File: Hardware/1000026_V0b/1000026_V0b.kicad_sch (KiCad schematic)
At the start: 29 parts, among them J1 533750410, J2 4390, J3 532580229, J5 532580229, J9 0525591853, SW1 TL3305CF260QG, U1 BD450M5FP-CE2, U2 MAX7480ESA+

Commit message: Updating lp filter test project
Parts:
- D1, D2: footprint RobotFtpLib:1N4007G-T -> DO-41_DIO
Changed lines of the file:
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@@
 			)
 		)
-		(property "Footprint" "RobotFtpLib:1N4007G-T"
+		(property "Footprint" "DO-41_DIO"
 			(at 95.504 127.381 0)
 			(effects
@@
 	)
 	(symbol
-		(lib_name "1N4007G-T_1")
 		(lib_id "RobotSymLib:1N4007G-T")
 		(at 93.7859 110.2875 0)
@@
 			)
 		)
-		(property "Footprint" "RobotFtpLib:1N4007G-T"
+		(property "Footprint" "DO-41_DIO"
 			(at 99.1199 103.6835 0)
 			(effects
@@
 			)
 		)
-		(property "Description" ""
+		(property "Description" "Power symbol creates a global label with name \"+7.4V\""
 			(at 23.8954 151.3699 0)
 			(effects

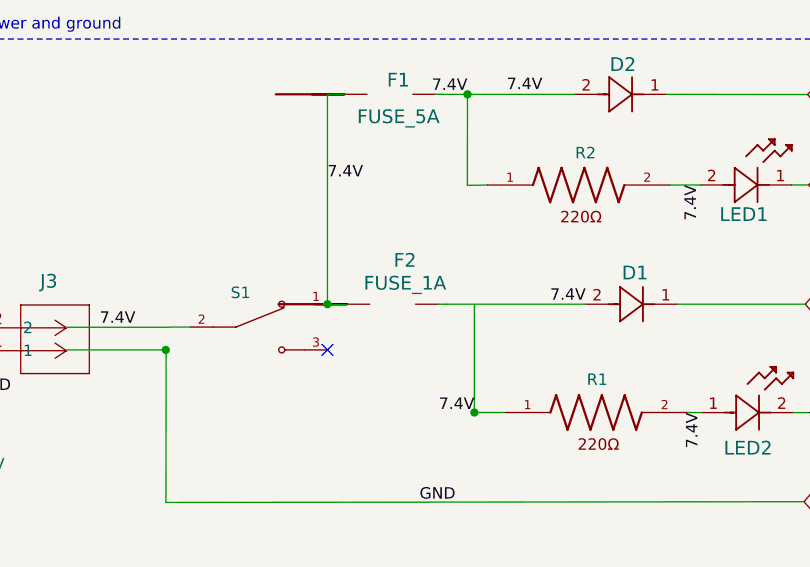
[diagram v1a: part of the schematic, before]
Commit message: Updating KiCad library
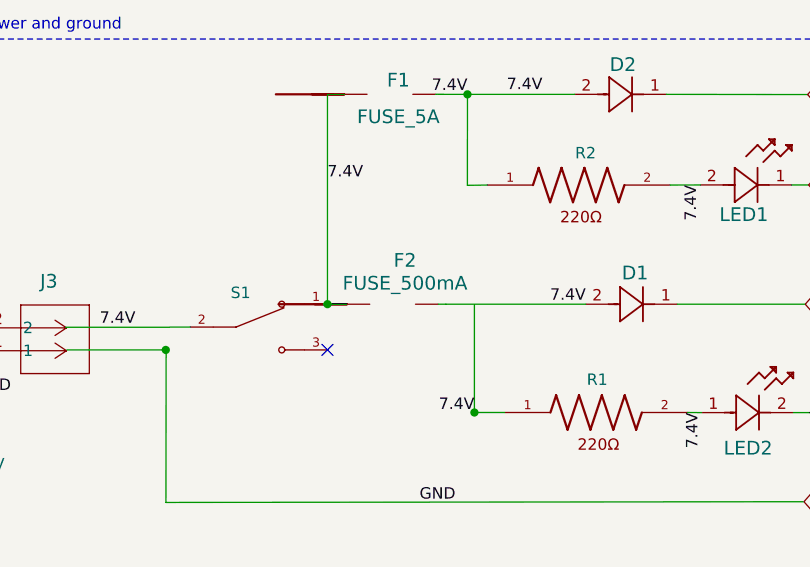
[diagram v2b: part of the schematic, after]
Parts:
- F2: value FUSE_1A -> FUSE_500mA
- J3: footprint RobotFtpLib:0532580229 -> CON_532580229_MOL
- S1: footprint RobotFtpLib:500SSP1S2M2QEA -> SW_500SSP1S2M2QEA
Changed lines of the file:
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@@
 	(generator "eeschema")
 	(generator_version "8.0")
-	(paper "A4")
+	(paper "USLetter")
 	(junction
 		(at 194.7164 137.2362)
@@
 			)
 		)
-		(property "Footprint" "RobotFtpLib:500SSP1S2M2QEA"
+		(property "Footprint" "SW_500SSP1S2M2QEA"
 			(at 56.896 147.32 0)
 			(effects
@@
 			)
 		)
-		(property "Value" "FUSE_1A"
+		(property "Value" "FUSE_500mA"
 			(at 74.909 131.2804 0)
 			(effects
@@
 	)
 	(symbol
+		(lib_name "532580229_1")
 		(lib_id "RobotSymLib:532580229")
 		(at 27.1334 138.7712 0)
@@
 			)
 		)
-		(property "Footprint" "RobotFtpLib:0532580229"
+		(property "Footprint" "CON_532580229_MOL"
 			(at 27.6414 148.4232 0)
 			(effects
@@
 			)
 		)
-		(property "Description" "Power symbol creates a global label with name \"+7.4V\""
+		(property "Description" "Power symbol creates a global label with name \"+9.0V\""
 			(at 23.8954 151.3699 0)
 			(effects
@@
 			)
 		)
-		(property "Description" ""
+		(property "Description" "Power symbol creates a global label with name \"GNDREF\" , reference supply ground"
 			(at 27.1334 145.6292 0)
 			(effects

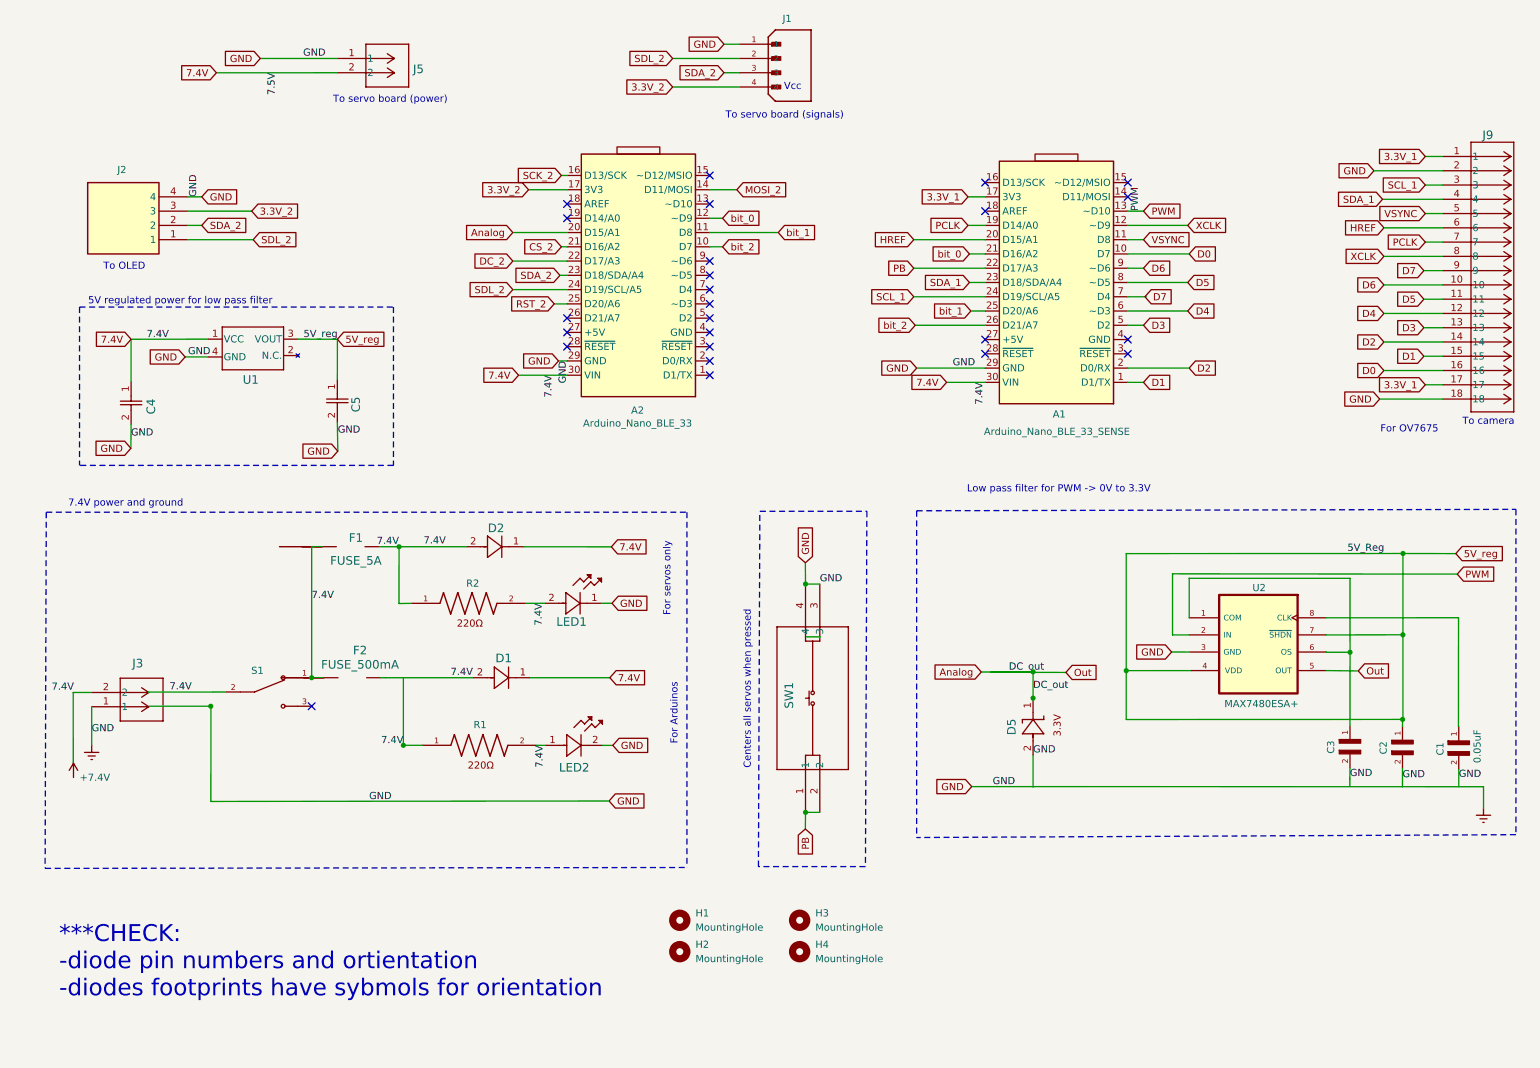
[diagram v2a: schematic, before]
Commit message: Updating KiCad library
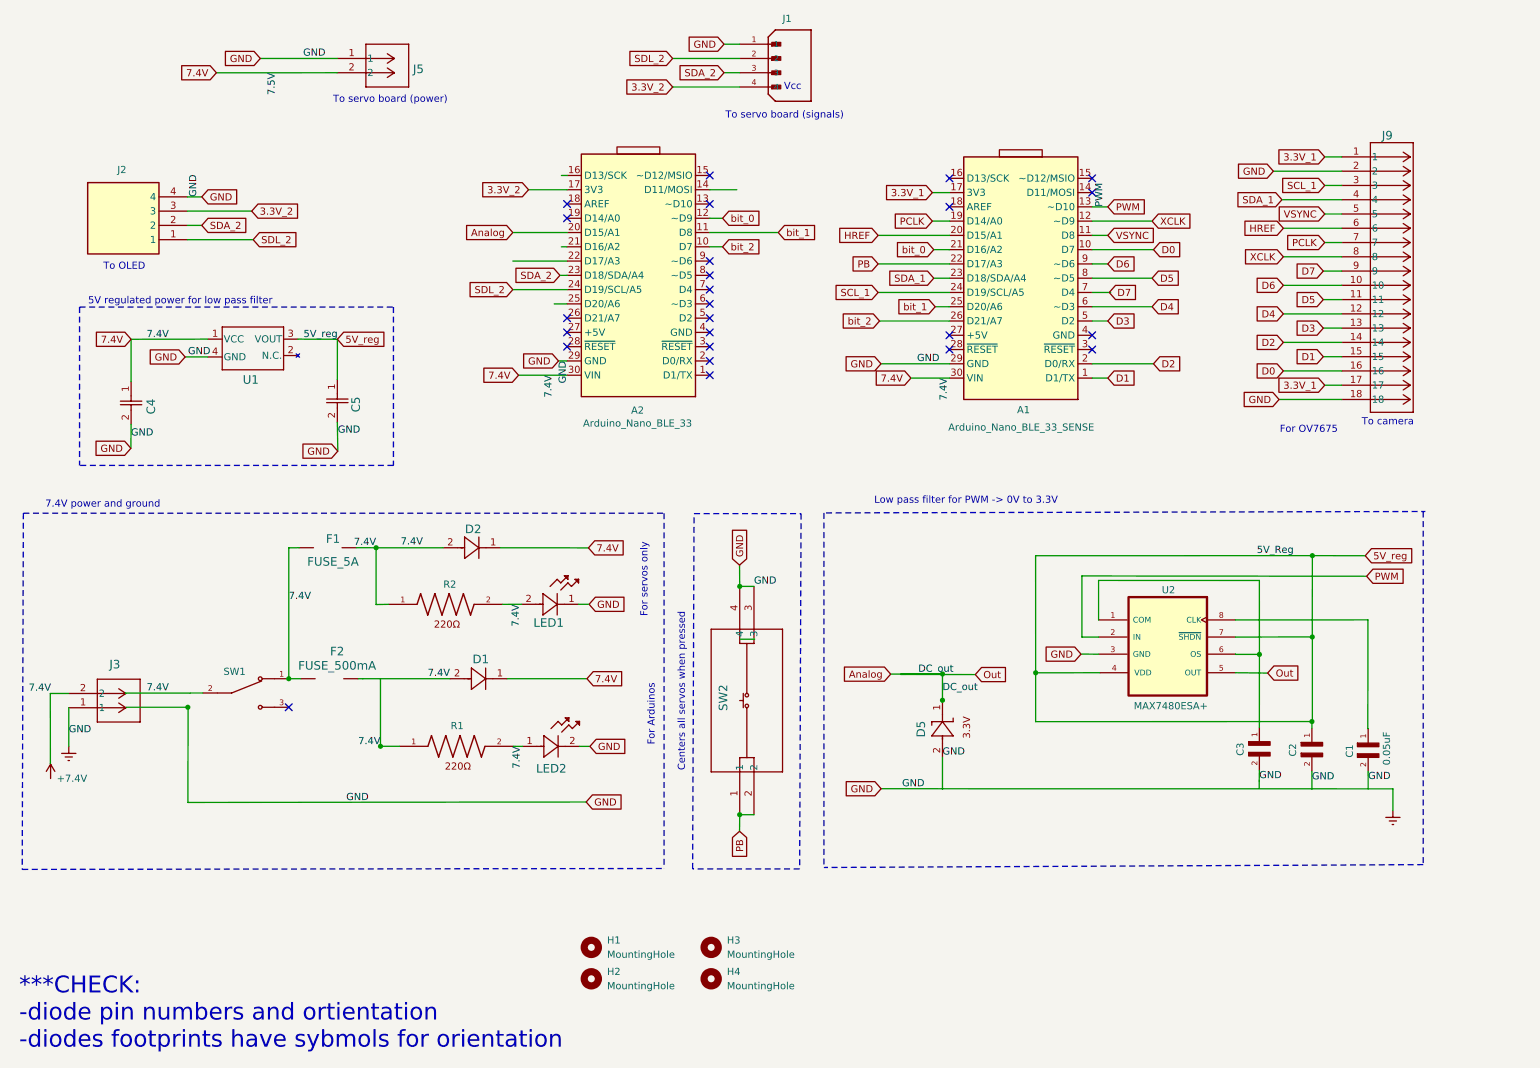
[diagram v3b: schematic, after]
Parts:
- J5: footprint RobotFtpLib:0532580229 -> CON_532580229_MOL
- renumbered S1 to SW1, SW1 to SW2
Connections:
- net CS_2: no longer names the net of A2.21 (D16/A2)
- net DC_2: no longer names the net of A2.22 (D17/A3)
- net MOSI_2: no longer names the net of A2.14 (D11/MOSI)
- net RST_2: no longer names the net of A2.25 (D20/A6)
- net SCK_2: no longer names the net of A2.16 (D13/SCK)
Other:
- moved on the sheet: A1, C1, C2, C3, D1, D2, D5, H1, H2, H3, H4, J3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

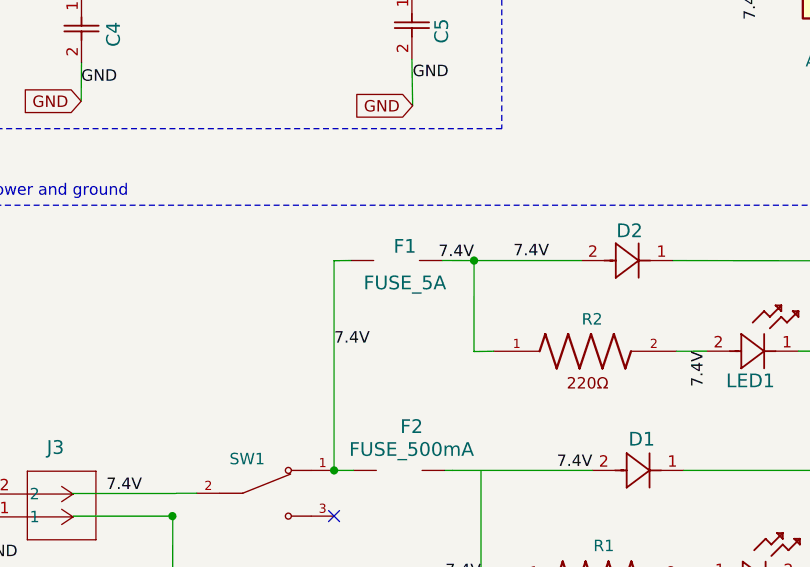
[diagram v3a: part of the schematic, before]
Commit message: Updating KiCad library
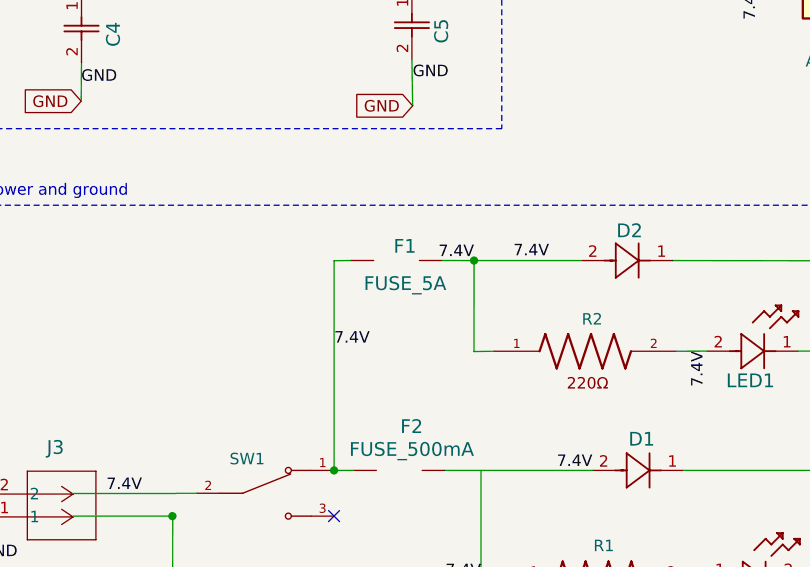
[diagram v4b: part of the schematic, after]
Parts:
- F1: footprint RobotFtpLib:RGEF300HF -> footprints:RGEF500HF
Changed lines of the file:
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@@
 		)
 		(property "Value" "FUSE_5A"
-			(at 70.0911 112.9554 0)
+			(at 70.104 113.03 0)
 			(effects
 				(font
@@
 			)
 		)
-		(property "Footprint" "RobotFtpLib:RGEF300HF"
+		(property "Footprint" "footprints:RGEF500HF"
 			(at 69.0322 119.7326 0)
 			(effects

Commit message: Updating Kicad library.
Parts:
- J3: symbol RobotSymLib:532580229 -> RobotLibrary:532580229
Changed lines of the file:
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@@
 	)
 	(symbol
-		(lib_id "RobotSymLib:532580229")
+		(lib_id "RobotLibrary:532580229")
 		(at 23.0565 138.9506 0)
 		(mirror x)
@@
 		)
 		(property "Footprint" "CON_532580229_MOL"
-			(at 23.5645 148.6026 0)
+			(at 24.5805 131.3306 0)
 			(effects
 				(font
@@
 		)
 		(property "Datasheet" "532580229"
-			(at 23.3105 143.7766 0)
+			(at 21.7865 142.7606 0)
 			(effects
 				(font
@@
 	)
 	(symbol
-		(lib_id "RobotSymLib:+7.4V")
+		(lib_id "RobotLibrary:+7.4V")
 		(at 19.8185 151.5493 0)
 		(unit 1)
@@
 		)
 		(property "Footprint" ""
-			(at 19.8185 151.5493 0)
+			(at 21.9775 153.9623 0)
 			(effects
 				(font
@@
 		)
 		(property "Datasheet" ""
-			(at 19.8185 151.5493 0)
+			(at 21.9775 153.9623 0)
 			(effects
 				(font

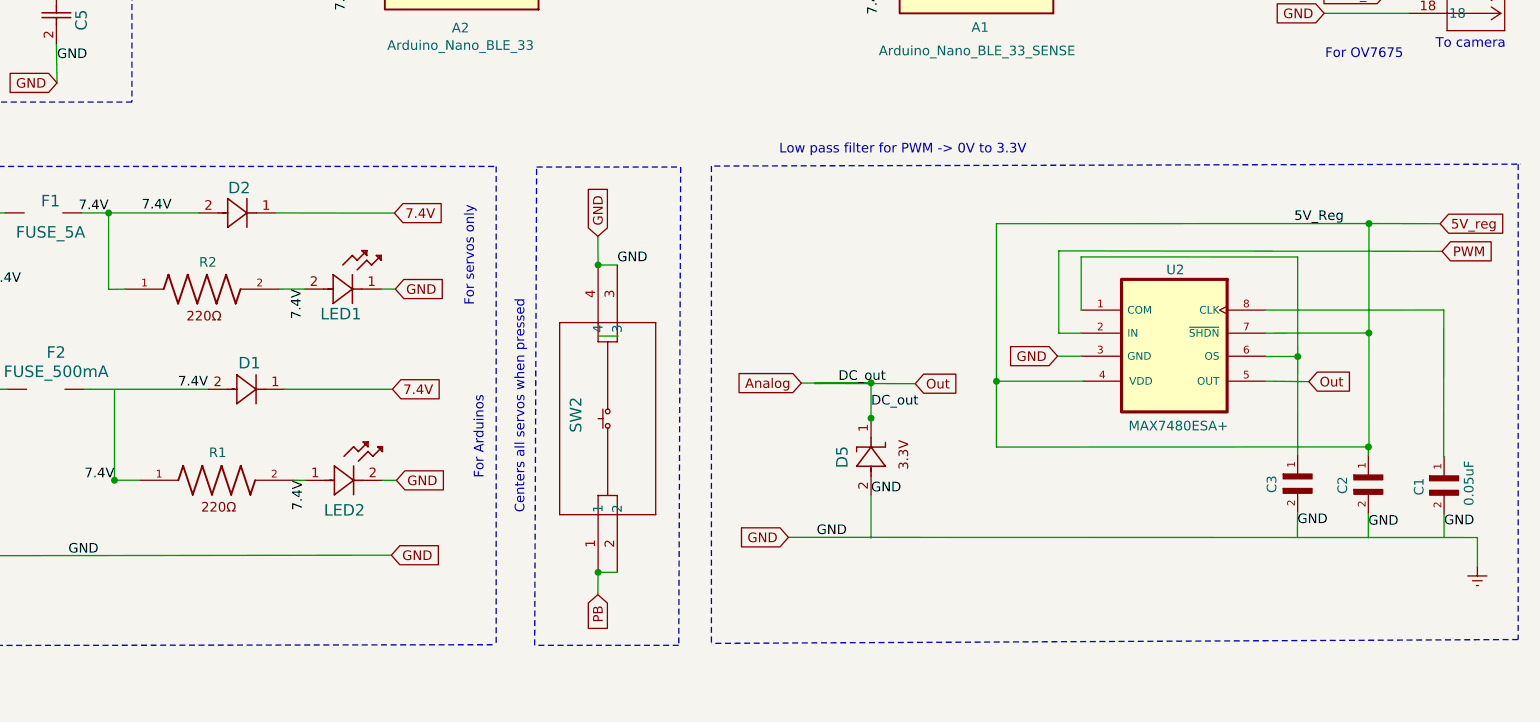
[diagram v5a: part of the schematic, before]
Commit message: Updating low pass filter schematic.
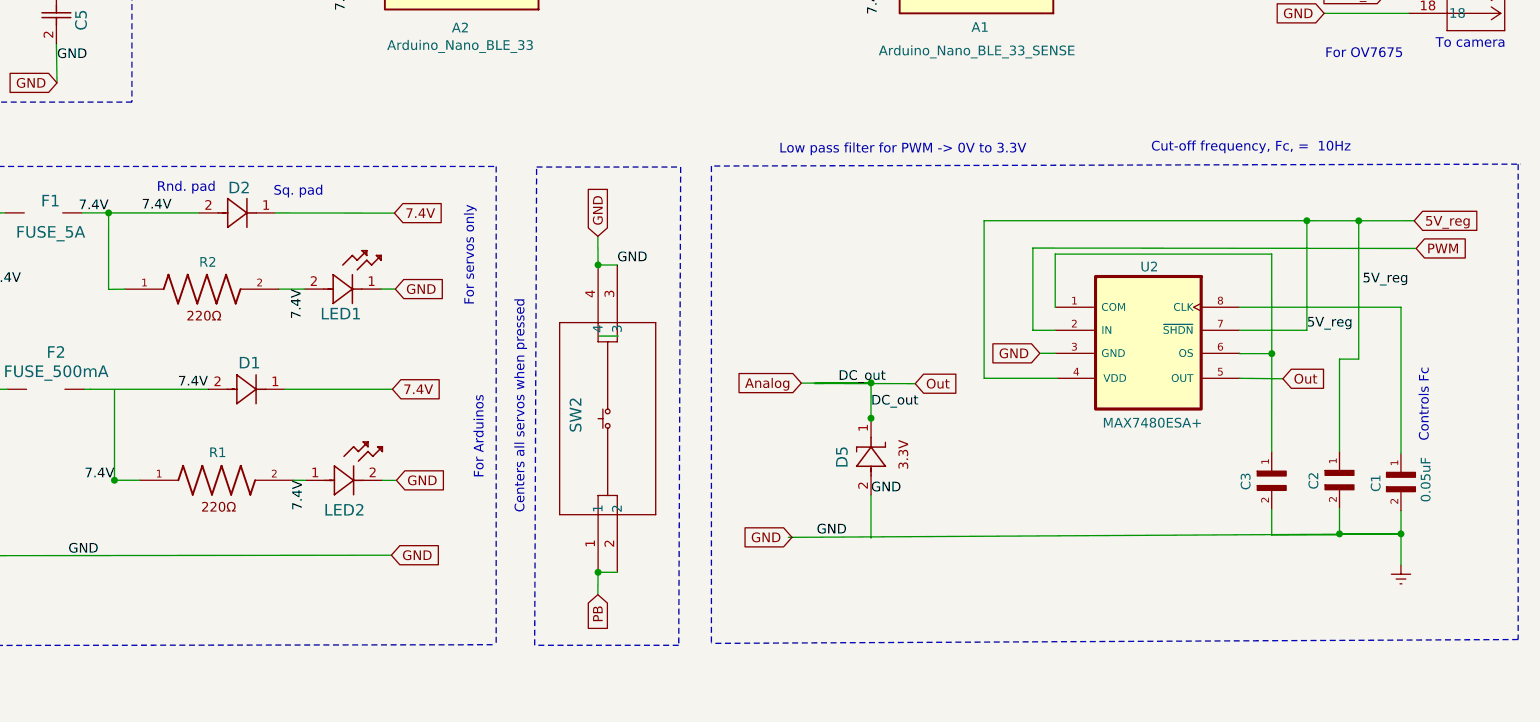
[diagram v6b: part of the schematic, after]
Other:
- note added: "Controls Fc"
- note added: "Cut-off frequency, Fc, = 10Hz"
- note added: "Rnd. pad"
- note added: "Sq. pad"
- moved on the sheet: C1, C2, C3, U2
